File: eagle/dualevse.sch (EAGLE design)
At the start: 54 parts, among them J2 I2C, J3 EXP, Q1 2N2222A, Q2 2N2222A, Q3 2N2222A, Q4 2N2222A, X1 RELAY, X2 CHARGE1, X3 CHARGE2, X4 RS485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

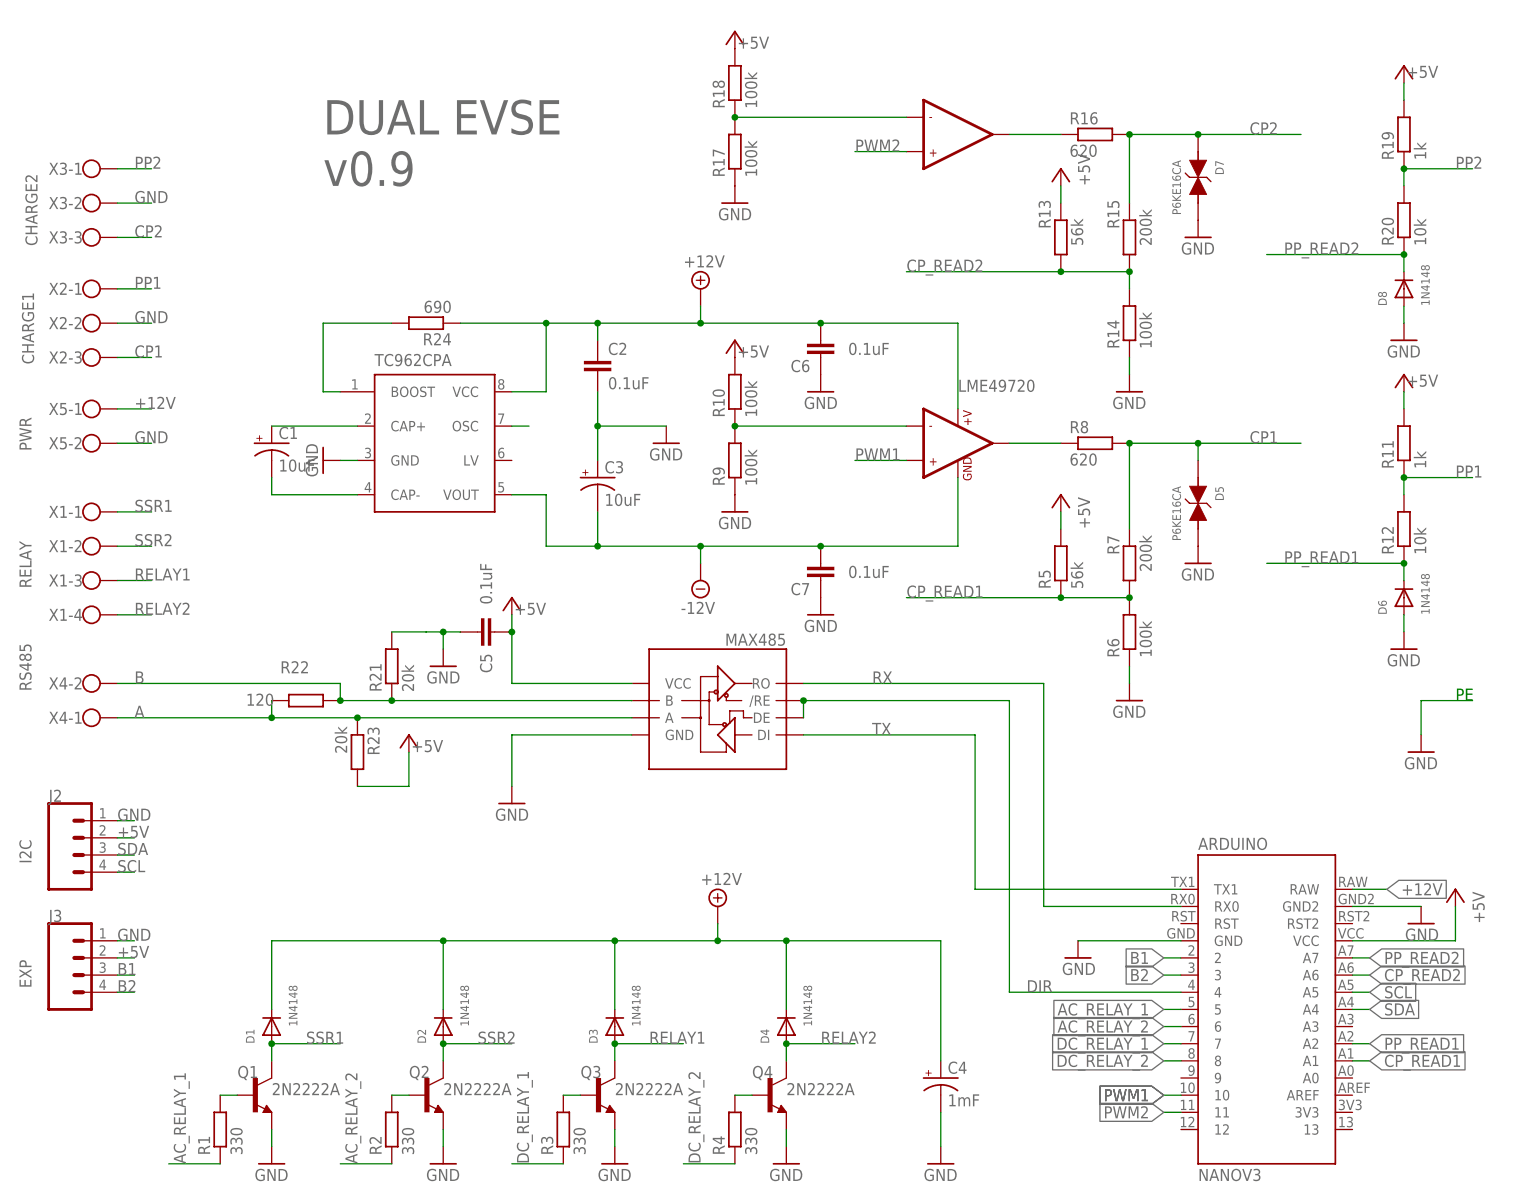
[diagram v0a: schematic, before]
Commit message: version 0.91
added 2 capacitors
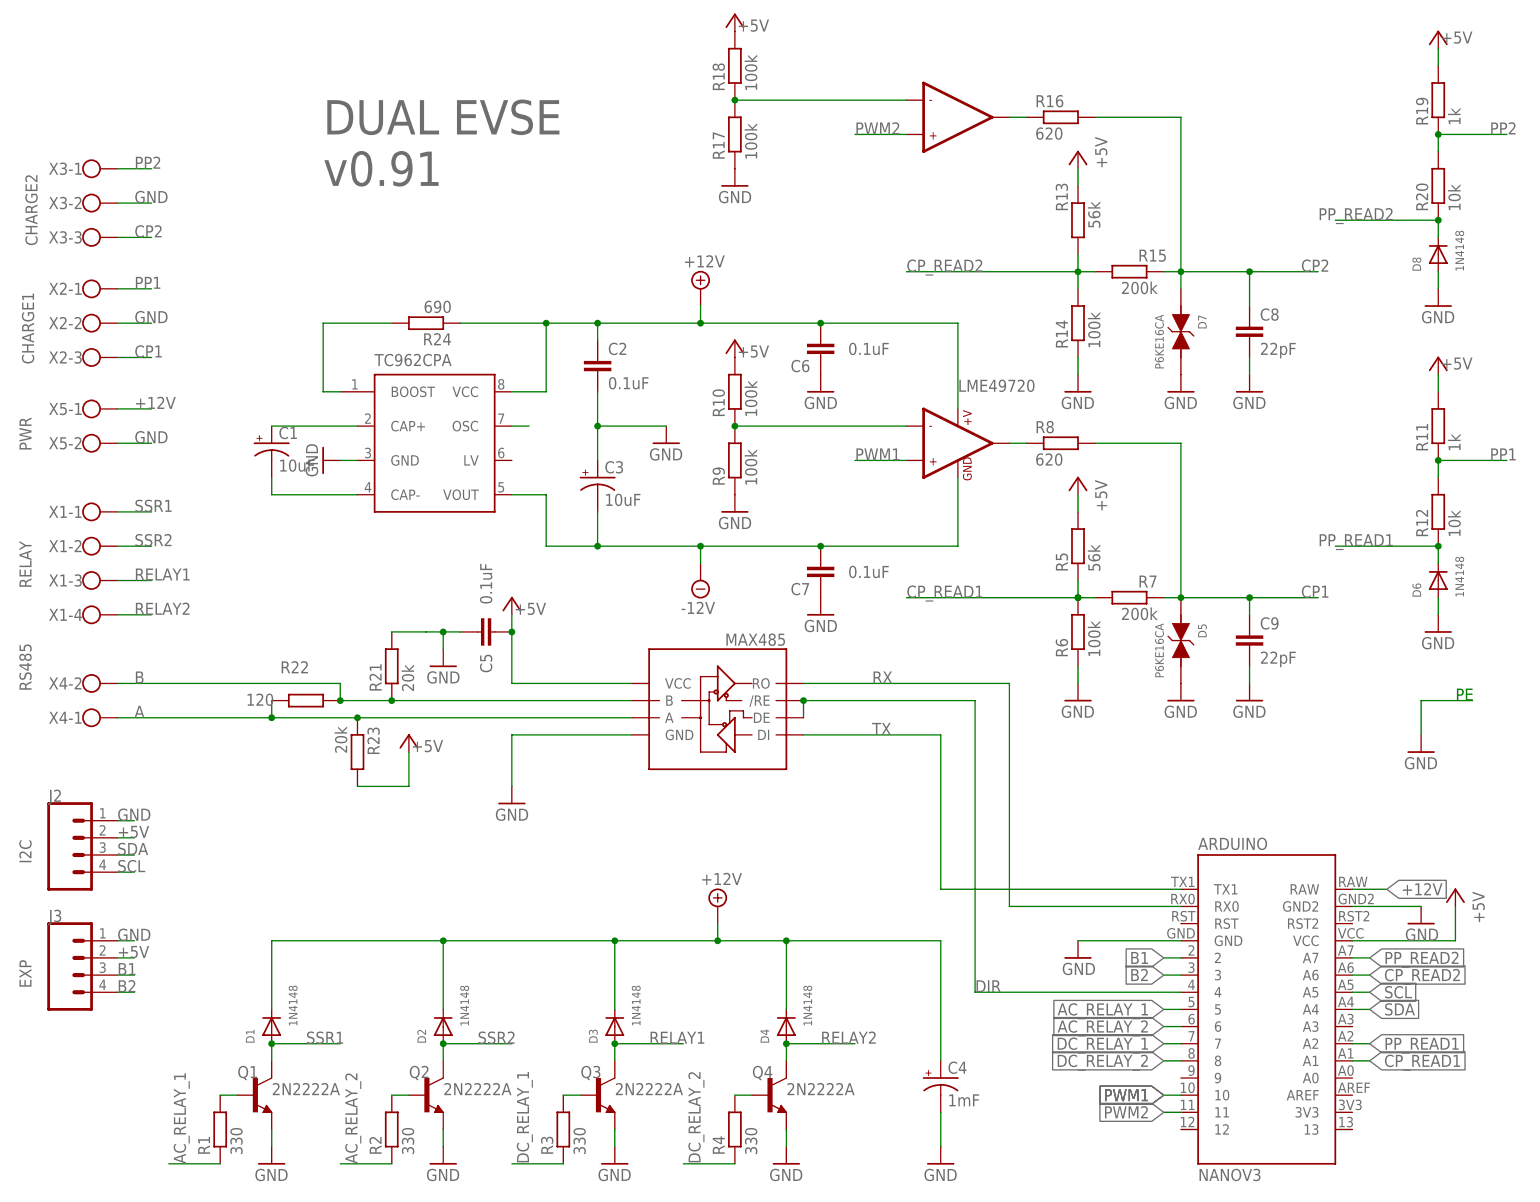
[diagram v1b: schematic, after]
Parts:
- added C8, C9: 22pF, SparkFun-Capacitors:22PF-PTH-2.54MM-200V-5%
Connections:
- net CP1: now also C9.1
- net CP2: now also C8.1
- net GND: now also C8.2, C9.2
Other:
- note added: "DUAL EVSE v0.91"
- note removed: "DUAL EVSE v0.9"
- moved on the sheet: D5, D6, D7, D8, R11, R12, R13, R14, R15, R16, R17, R18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
